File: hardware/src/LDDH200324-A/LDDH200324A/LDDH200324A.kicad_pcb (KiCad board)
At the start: 2 copper layers, 30 x 30 mm, 126 parts, among them J1 Conn_01x03, J2 Conn_01x03, J3 Conn_01x03, J4 Conn_01x03

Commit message: Inicia a implementação do firmware. Implementa a Biblioteca de RTC.
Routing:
- net PIN_12: track 24.3 -> 43.9 mm, vias 4 -> 7
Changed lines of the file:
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@@
     (thickness 1.6)
     (drawings 473)
-    (tracks 512)
+    (tracks 528)
     (zones 0)
     (modules 126)
@@
   (segment (start 138.44582 98.5346) (end 139.2456 98.5346) (width 0.3) (layer F.Cu) (net 4))
   (segment (start 137.00786 97.09664) (end 138.44582 98.5346) (width 0.3) (layer F.Cu) (net 4))
-  (segment (start 141.110688 101.1901) (end 141.215022 101.1901) (width 0.3) (layer F.Cu) (net 12))
   (via (at 139.652 100.442) (size 0.6) (drill 0.3) (layers F.Cu B.Cu) (net 4))
   (segment (start 140.374978 100.7353) (end 139.9453 100.7353) (width 0.3) (layer F.Cu) (net 4))
@@
   (segment (start 150.447 108.062) (end 150.193 107.808) (width 0.3) (layer B.Cu) (net 8))
   (segment (start 150.193 107.808) (end 147.124608 107.808) (width 0.3) (layer B.Cu) (net 8))
+  (segment (start 137.2239 105.4585) (end 136.6675 105.4585) (width 0.3) (layer F.Cu) (net 8))
+  (via (at 136.477 105.649) (size 0.6) (drill 0.3) (layers F.Cu B.Cu) (net 8))
+  (segment (start 136.6675 105.4585) (end 136.477 105.649) (width 0.3) (layer F.Cu) (net 8))
+  (segment (start 136.477 105.649) (end 139.271 108.443) (width 0.3) (layer B.Cu) (net 8))
+  (via (at 143.081 108.443) (size 0.6) (drill 0.3) (layers F.Cu B.Cu) (net 8))
+  (segment (start 139.271 108.443) (end 143.081 108.443) (width 0.3) (layer B.Cu) (net 8))
+  (segment (start 143.081 108.6438) (end 142.7254 108.9994) (width 0.3) (layer F.Cu) (net 8))
+  (segment (start 143.081 108.443) (end 143.081 108.6438) (width 0.3) (layer F.Cu) (net 8))
+  (via (at 132.032 108.57) (size 0.6) (drill 0.3) (layers F.Cu B.Cu) (net 8))
+  (segment (start 134.064 108.443) (end 132.159 108.443) (width 0.3) (layer F.Cu) (net 8))
+  (segment (start 136.223 106.284) (end 134.064 108.443) (width 0.3) (layer F.Cu) (net 8))
+  (segment (start 132.159 108.443) (end 132.032 108.57) (width 0.3) (layer F.Cu) (net 8))
+  (segment (start 136.477 105.649) (end 136.223 105.903) (width 0.3) (layer F.Cu) (net 8))
+  (segment (start 136.223 105.903) (end 136.223 106.284) (width 0.3) (layer F.Cu) (net 8))
+  (segment (start 131.905 108.697) (end 131.905 113.015) (width 0.3) (layer B.Cu) (net 8))
+  (segment (start 132.032 108.57) (end 131.905 108.697) (width 0.3) (layer B.Cu) (net 8))
   (segment (start 142.358022 104.1746) (end 142.370722 104.1619) (width 0.3) (layer F.Cu) (net 9))
   (segment (start 142.358022 105.2795) (end 142.358022 104.1746) (width 0.3) (layer F.Cu) (net 9))
@@
   (segment (start 154.8134 109.6344) (end 154.003 108.824) (width 0.3) (layer F.Cu) (net 11))
   (segment (start 156.15184 109.6344) (end 154.8134 109.6344) (width 0.3) (layer F.Cu) (net 11))
+  (segment (start 141.110688 101.1901) (end 141.215022 101.1901) (width 0.3) (layer F.Cu) (net 12))
   (segment (start 148.3896 101.7652) (end 148.8468 101.7652) (width 0.3) (layer F.Cu) (net 12))
   (segment (start 141.159195 101.134273) (end 141.215022 101.1901) (width 0.3) (layer F.Cu) (net 12))

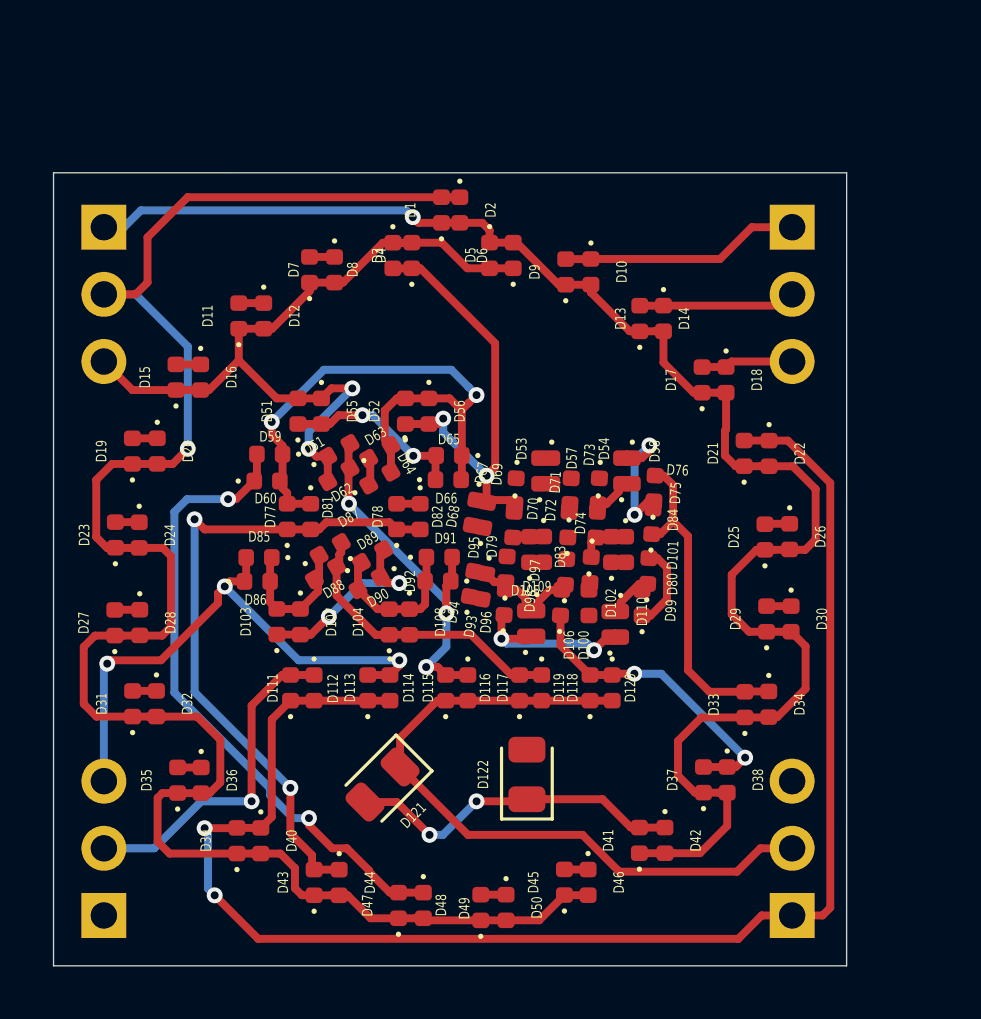
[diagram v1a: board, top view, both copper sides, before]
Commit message: Atualiza o modelo do Display. Inicia a implementação da biblioteca de Charlieplexing.
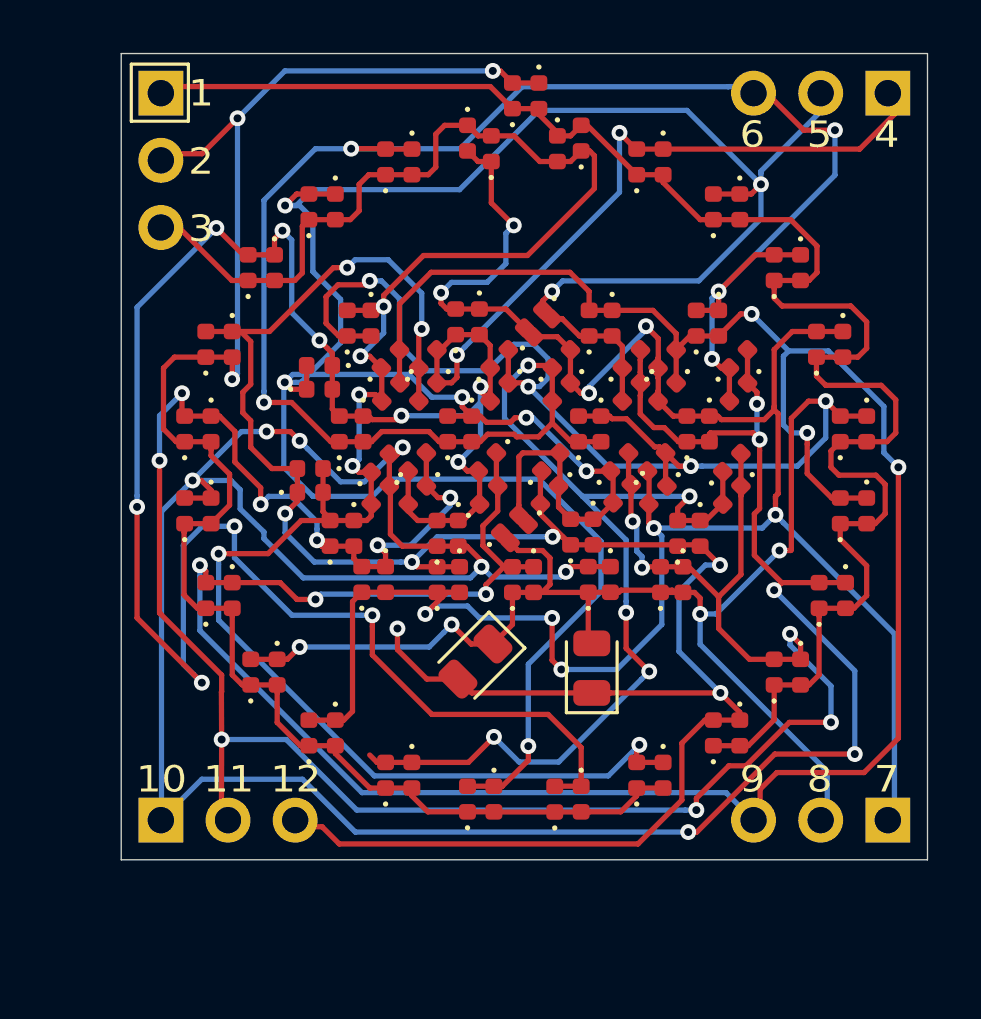
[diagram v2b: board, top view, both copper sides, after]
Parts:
- moved D67 7.64 mm to (148.2, 95.5), turned to 225 degrees
- moved D68 7.47 mm to (148.5, 95.9), turned to 45 degrees
- moved D58 6.47 mm to (155.2, 95.7)
- moved D54 6.26 mm to (154.3, 95.7)
- moved J2 6.23 mm to (161.6, 87.0), turned to 90 degrees
- moved D53 6.23 mm to (151.1, 95.7), turned to 270 degrees
- moved D76 5.88 mm to (155.9, 98.3), turned to 225 degrees
- moved D75 5.84 mm to (155.9, 97.0), turned to 45 degrees
- moved D121 5.83 mm to (146.0, 108.5)
- moved D57 5.77 mm to (150.3, 95.7), turned to 90 degrees
- moved D74 5.68 mm to (153.2, 98.3), turned to 225 degrees
- moved D73 5.63 mm to (153.2, 97.0), turned to 45 degrees
- moved D96 5.58 mm to (148.8, 100.9), turned to 45 degrees
- moved D72 5.56 mm to (151.9, 98.3), turned to 225 degrees
- moved D84 5.55 mm to (154.8, 99.7)
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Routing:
- net PIN_10: track 24.5 -> 108.5 mm, vias 0 -> 11
- net PIN_09: track 18.7 -> 101.1 mm, vias 3 -> 6
- net PIN_05: track 38.4 -> 111.6 mm, vias 2 -> 8
- net PIN_04: track 39.1 -> 107.0 mm, vias 2 -> 12
- net PIN_06: track 38.2 -> 104.9 mm, vias 4 -> 10
- net PIN_08: track 35.3 -> 88.7 mm, vias 2 -> 8
- net PIN_11: track 35.9 -> 87.0 mm, vias 5 -> 12
- net PIN_12: track 43.9 -> 88.5 mm, vias 7 -> 8
- net PIN_03: track 35.5 -> 78.1 mm, vias 2 -> 6
- net PIN_07: track 78.1 -> 85.2 mm, vias 4 -> 9
- net PIN_01: track 60.3 -> 66.1 mm, vias 1 -> 0
- net PIN_02: track 71.5 -> 66.0 mm, vias 1 -> 3
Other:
- board size 30 x 30 mm -> 30.5 x 30.5 mm
- net class Default: clearance 0.254 -> 0.2; trace_width 0.3 -> 0.2
- rule trace_clearance: 0.254 -> 0.2
- board text added: "1"
- board text added: "10"
- board text added: "11"
- board text added: "12"
- board text added: "2"
- board text added: "3"
- board text added: "4"
- board text added: "5"
- board text added: "6"
- board text added: "7"
- board text added: "8"
- board text added: "9"
- board text added: "H.Orloj Display"
- board text added: "P"
- board text added: "P/N: LDDH200324A"
